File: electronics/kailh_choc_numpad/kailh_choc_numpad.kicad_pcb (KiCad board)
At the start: 2 copper layers, 100 x 88 mm, 117 parts, among them J1 Conn_01x06

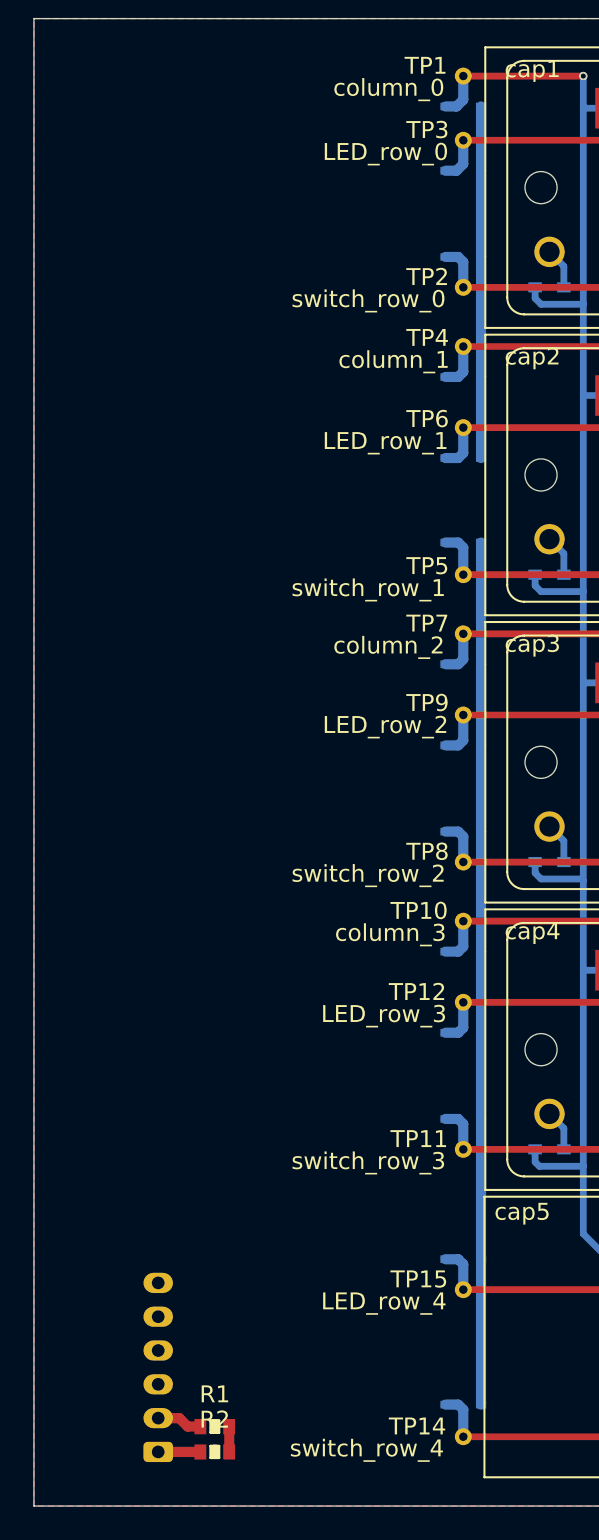
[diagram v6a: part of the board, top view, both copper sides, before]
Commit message: added i2c port expander but wrong footprint, now
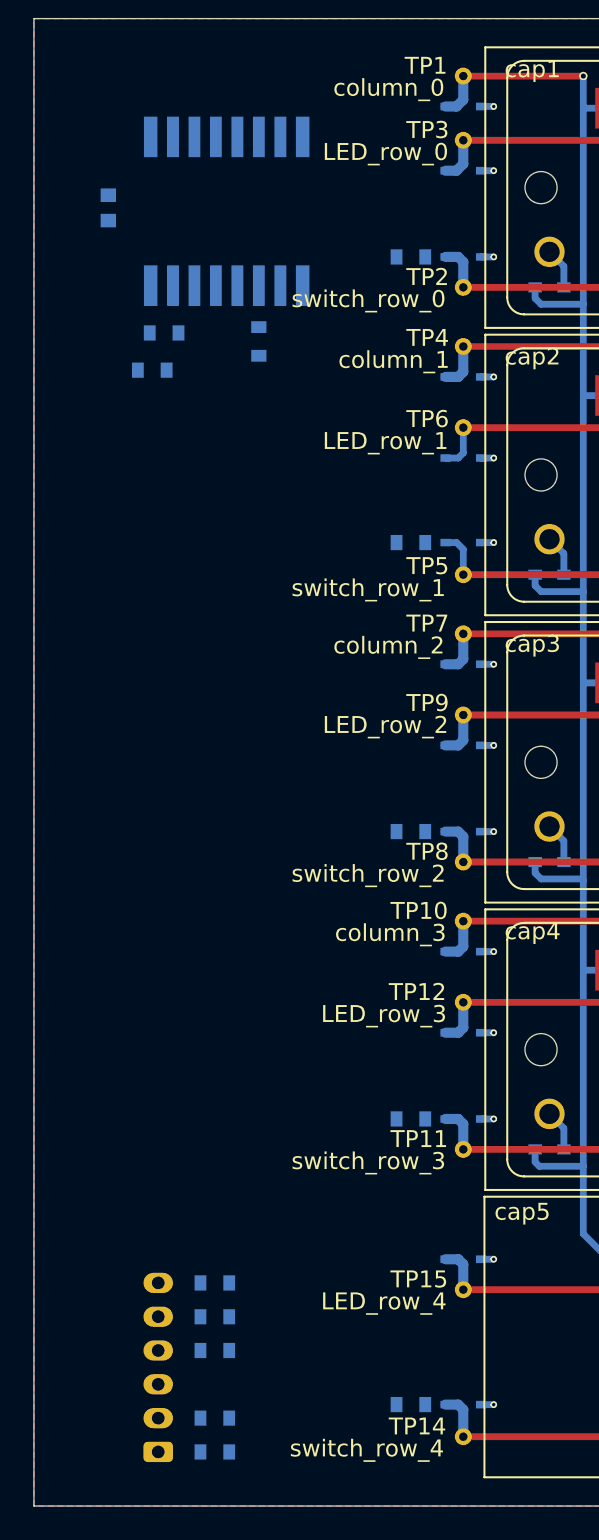
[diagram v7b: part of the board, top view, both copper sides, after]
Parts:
- added C1: 1u, SquantorRcl:C_0603, B.Cu at (138.9, 81.2)
- added R20: 100, SquantorRcl:R_0603_hand, B.Cu at (145.2, 144.8)
- added R21: 100, SquantorRcl:R_0603_hand, B.Cu at (145.2, 146.8)
- added R22: 100, SquantorRcl:R_0603_hand, B.Cu at (145.2, 148.8)
- added R23: 4.7K, SquantorRcl:R_0603_hand, B.Cu at (156.8, 84.1)
- added R24: 4.7K, SquantorRcl:R_0603_hand, B.Cu at (156.8, 101.0)
- added R25: 4.7K, SquantorRcl:R_0603_hand, B.Cu at (156.8, 118.1)
- added R26: 4.7K, SquantorRcl:R_0603_hand, B.Cu at (156.8, 135.1)
- added R27: 4.7K, SquantorRcl:R_0603_hand, B.Cu at (156.8, 152.0)
- added R28: 4.7K, SquantorRcl:R_0603_hand, B.Cu at (141.5, 90.8)
- added R29: 4.7K, SquantorRcl:R_0603_hand, B.Cu at (147.8, 89.1)
- added R30: 4.7K, SquantorRcl:R_0603_hand, B.Cu at (142.2, 88.6)
- added U1: PCA9554, SquantorIC:SOT162-1-NXP, B.Cu at (145.9, 81.4)
- R1, R2: moved to B.Cu
- moved R1 0.50 mm to (145.2, 152.8)
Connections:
- J1 pad 4: unconnected-(J1-Pad4) -> Net-(J1-Pad4)
- J1 pad 5: unconnected-(J1-Pad5) -> Net-(J1-Pad5)
- J1 pad 6: unconnected-(J1-Pad6) -> Net-(J1-Pad6)
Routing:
- net VSS: track 71.8 -> 10.5 mm, vias 0 -> 14
- net Net-(J1-Pad2): track 2.71 -> 0.00 mm
- net Net-(J1-Pad1): track 2.50 -> 0.00 mm
- net VDD: track 1.50 -> 0.00 mm

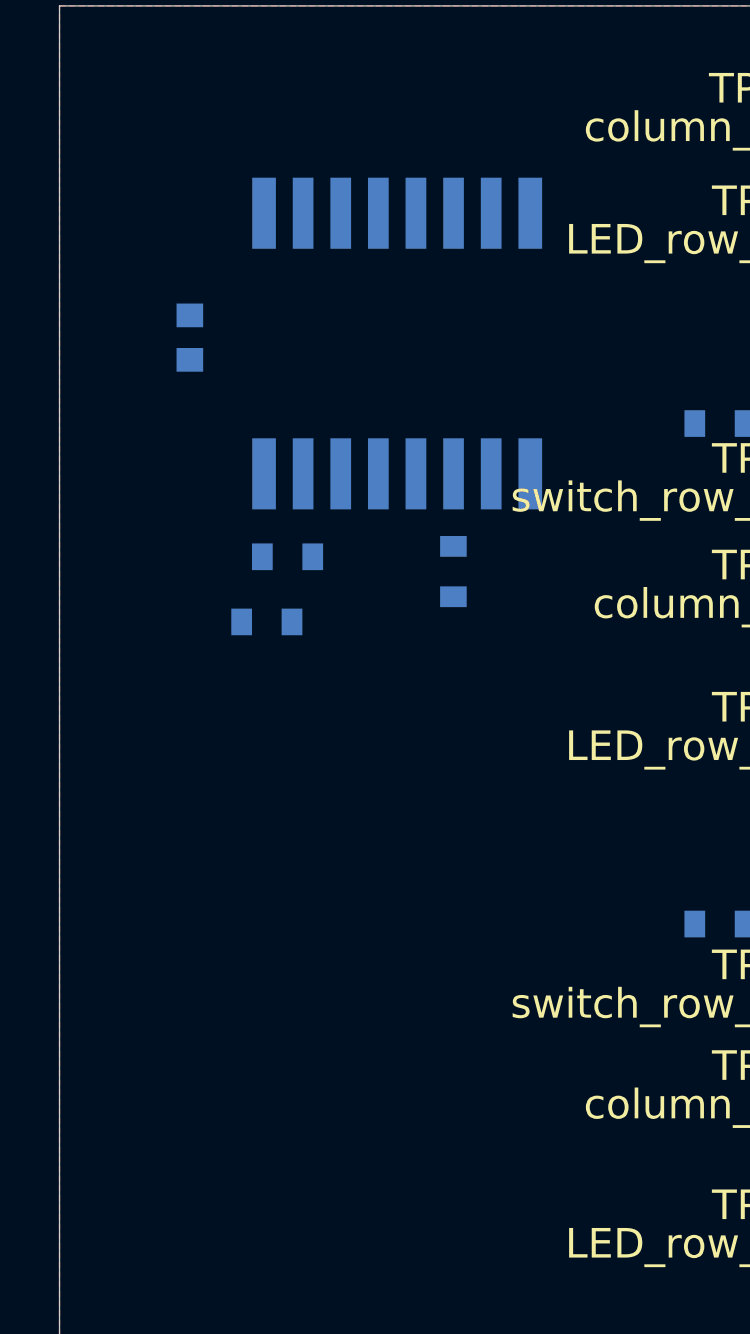
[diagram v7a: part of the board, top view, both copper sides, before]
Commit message: imported I2C expanders, time to route
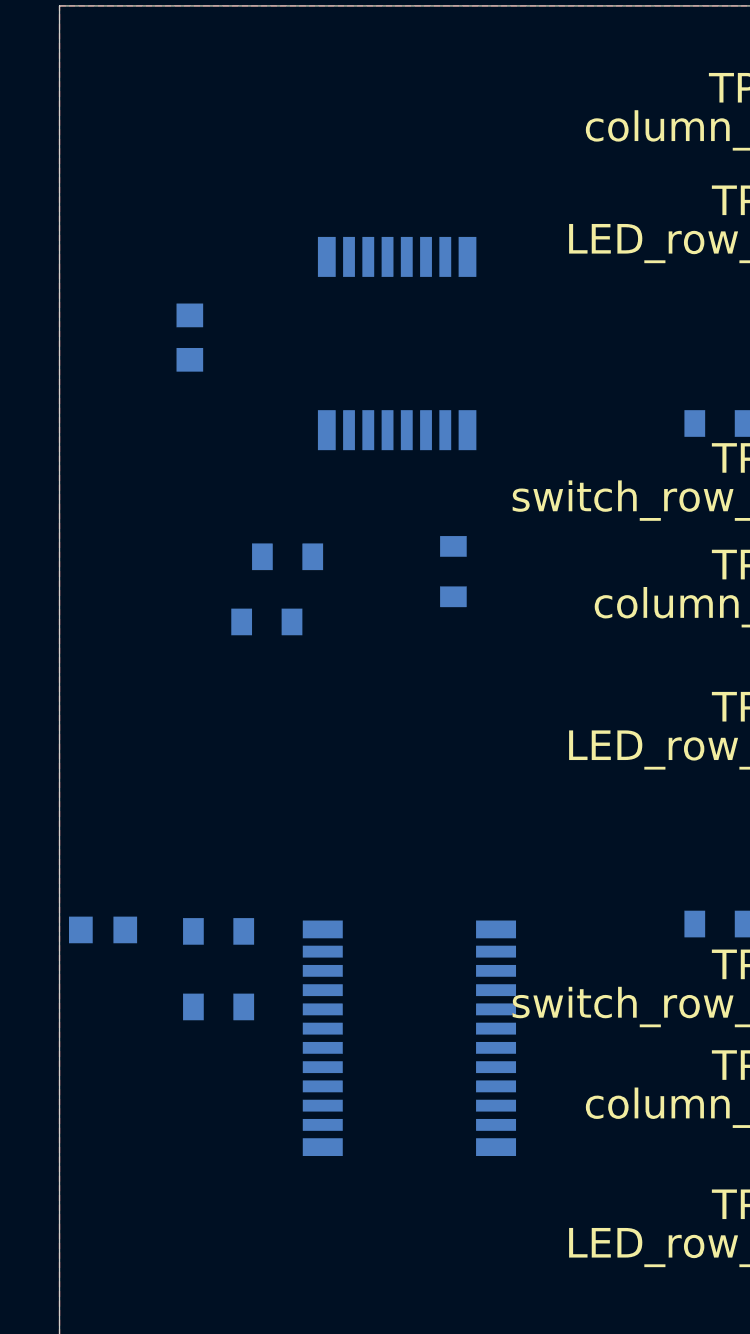
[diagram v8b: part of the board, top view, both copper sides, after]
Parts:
- added C2: 1u, SquantorRcl:C_0603, B.Cu at (136.0, 101.2)
- added R31: 4.7K, SquantorRcl:R_0603_hand, B.Cu at (139.9, 101.2)
- added R32: 4.7K, SquantorRcl:R_0603_hand, B.Cu at (139.9, 103.8)
- added U2: PCA9535, SquantorIC:SOT355-1-NXP, B.Cu at (146.3, 104.9)
- U1: footprint SquantorIC:SOT162-1-NXP -> SquantorIC:SOT403-1-NXP
